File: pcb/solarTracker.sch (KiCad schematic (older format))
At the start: 11 parts, among them U1 photodiode, U2 photodiode, U3 MCP6494, U4 photodiode, U5 photodiode

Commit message: use stm32d100 mcu, switch between four analog inputs using multiplexer, separate analog and digital gnds
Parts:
- added C3, C4, C5, C6, C7: C, symbol C
- added U6: STM32F071CBT6, symbol STM32F071CBT6
- U1, U2, U4, U5: symbol photodiode -> photodiode-RESCUE-solarTracker
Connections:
- net labels added: +BATT, DIO1, DIO2, DIO3, DIO4
- wire segments 47 -> 50
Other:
- moved on the sheet: C1, C2, R1, R2, R3, R4

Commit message: add 2nd order Butterworth filter, change first amp to lm324
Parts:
- removed R1, R2, R3, R4: UNREGULATED, symbol R
- removed U1, U2, U4, U5: photodiode, symbol photodiode-RESCUE-solarTracker
- removed U3: MCP6494, symbol MCP6494
- added C3, C4, C5: C, symbol C
- added U1: 74HC4052, symbol 74HC4052
- C2: value 100n -> C
- renumbered C7 to C10, C3 to C6, C4 to C7, C5 to C8, C6 to C9, U6 to U2
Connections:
- net labels added: GNDA
- net labels removed: +BATT, DIO1, DIO2, DIO3, DIO4, GND
- wire segments 50 -> 54
- no-connect marks 0 -> 5
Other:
- moved on the sheet: C10, C6, C7, C8, C9, U2

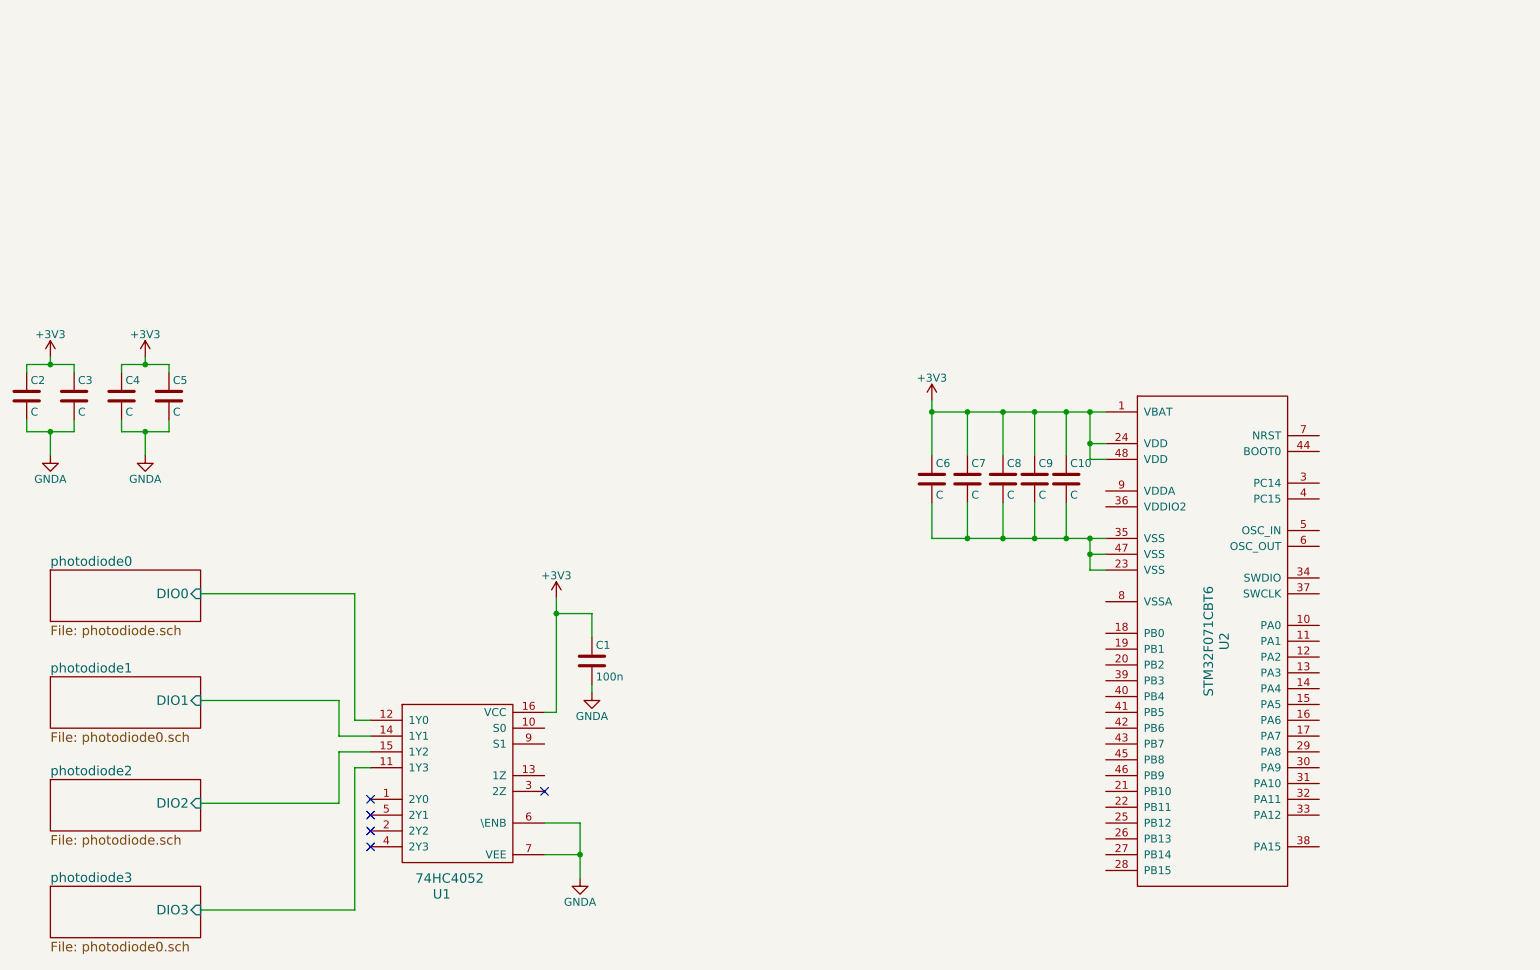
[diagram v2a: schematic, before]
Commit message: fix hierachal sheet labelling
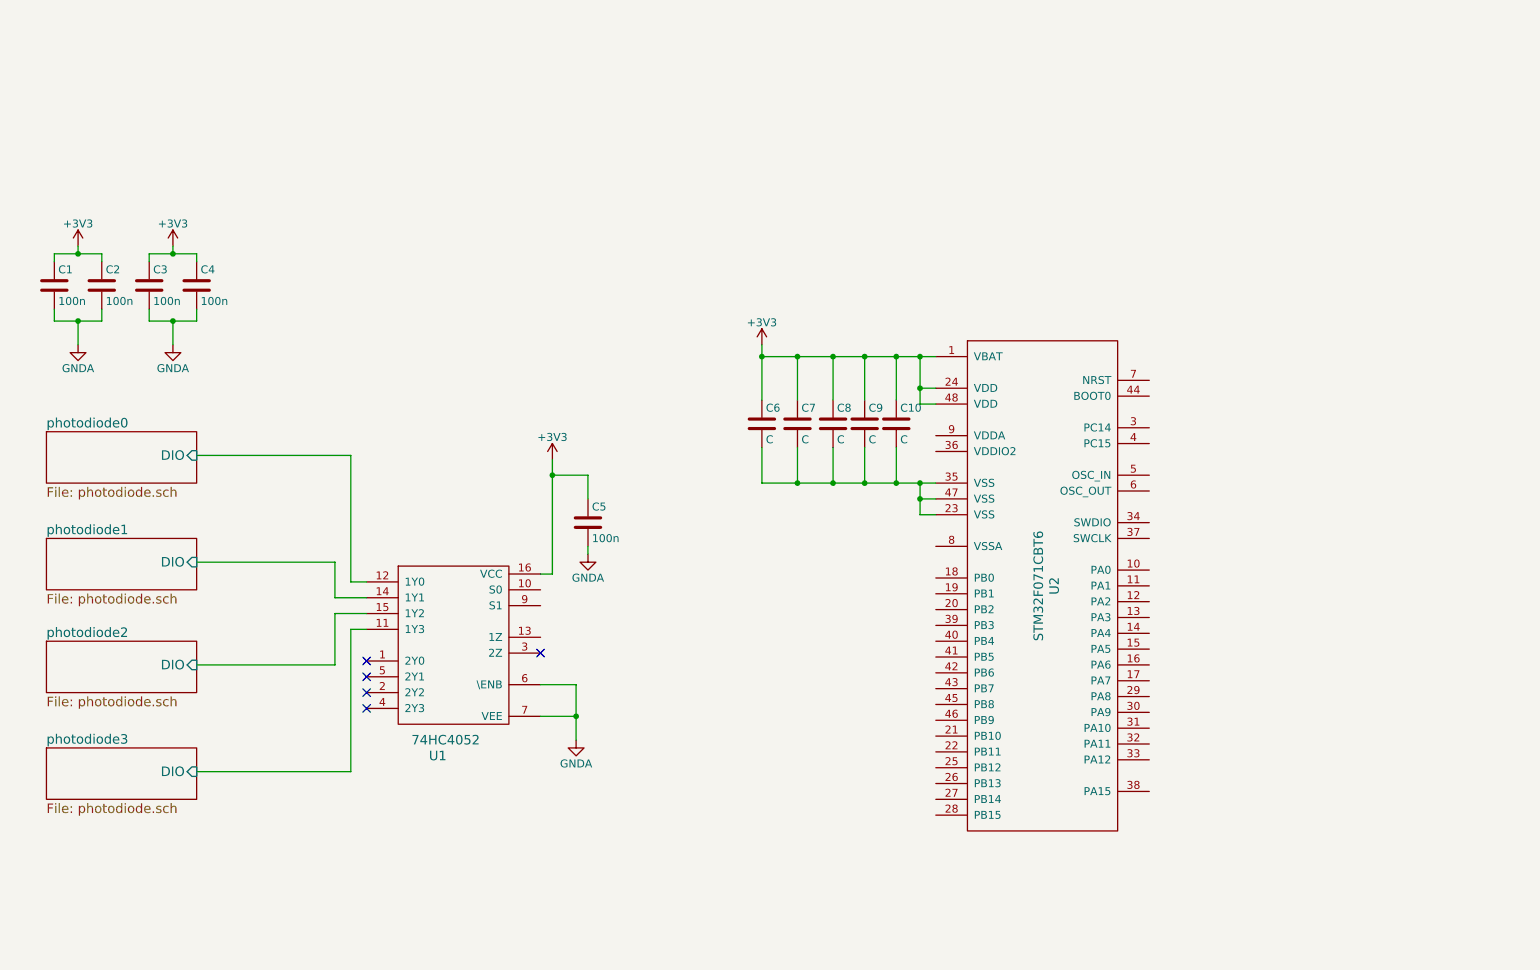
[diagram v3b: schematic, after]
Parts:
- C1: renamed from C2; value C -> 100n
- C2: renamed from C3; value C -> 100n
- C3: renamed from C4; value C -> 100n
- C4: renamed from C5; value C -> 100n
- renumbered C1 to C5
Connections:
- net photodiode0/DIO0 renamed photodiode0/DIO
- net photodiode1/DIO1 renamed photodiode1/DIO
- net photodiode2/DIO2 renamed photodiode2/DIO
- net photodiode3/DIO3 renamed photodiode3/DIO
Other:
- moved on the sheet: C1, C10, C2, C3, C4, C5, C6, C7, C8, C9, U1, U2

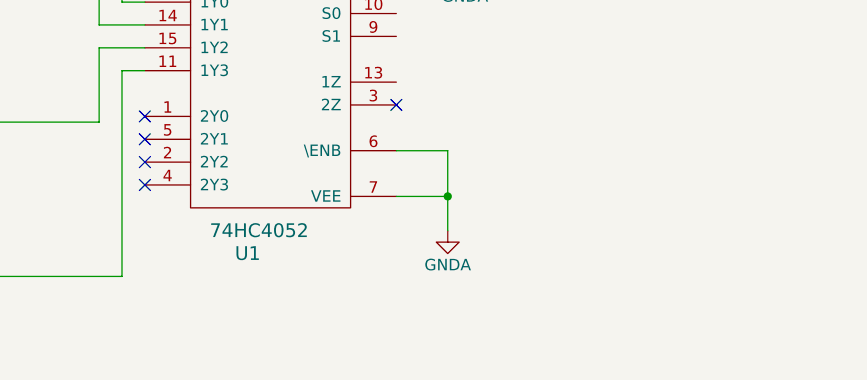
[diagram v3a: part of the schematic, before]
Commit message: change filter resistor to correct value, reduce cap size (and cost)
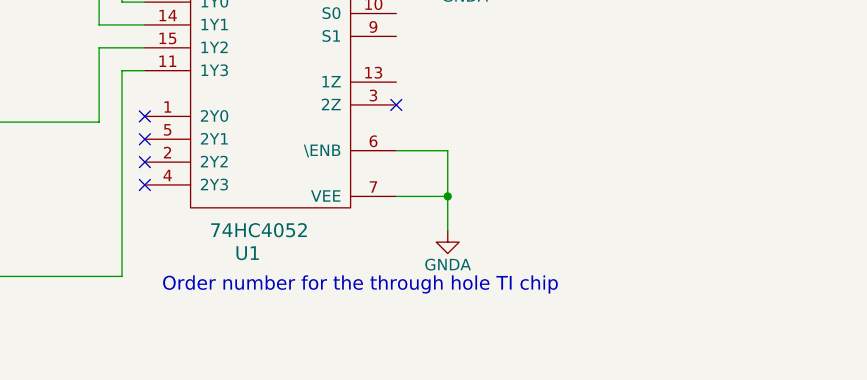
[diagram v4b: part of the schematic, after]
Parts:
- C3: Order No (none) -> 2468845; Supplier (none) -> Farnell
- U1: Order No (none) -> 1740159; Supplier (none) -> Farnell
- U2: Order No (none) -> 2376483; Supplier (none) -> Farnell
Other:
- note added: "Order number for the through hole TI chip"
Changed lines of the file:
@@
 F 2 "" H 7600 4725 60  0000 C CNN
 F 3 "" H 7600 4725 60  0000 C CNN
+F 4 "Farnell" V 7600 4525 60  0001 C CNN "Supplier"
+F 5 "2376483" V 7600 4525 60  0001 C CNN "Order No"
 	1    7600 4525
 	1    0    0    -1
@@
 F 2 "" H 3750 5450 60  0000 C CNN
 F 3 "" H 3750 5450 60  0000 C CNN
+F 4 "Farnell" H 3750 5450 60  0001 C CNN "Supplier"
+F 5 "1740159" H 3750 5450 60  0001 C CNN "Order No"
 	1    3750 5450
 	1    0    0    -1
 $EndComp
 $Comp
-L +3V3 #PWR5
+L +3V3 #PWR01
 U 1 1 55BCF6B7
 P 4475 3575
-F 0 "#PWR5" H 4475 3425 50  0001 C CNN
+F 0 "#PWR01" H 4475 3425 50  0001 C CNN
 F 1 "+3V3" H 4475 3715 50  0000 C CNN
 F 2 "" H 4475 3575 60  0000 C CNN
@@
 NoConn ~ 4400 4800
 $Comp
-L +3V3 #PWR8
+L +3V3 #PWR02
 U 1 1 55BD10C3
 P 5800 2850
-F 0 "#PWR8" H 5800 2700 50  0001 C CNN
+F 0 "#PWR02" H 5800 2700 50  0001 C CNN
 F 1 "+3V3" H 5800 2990 50  0000 C CNN
 F 2 "" H 5800 2850 60  0000 C CNN
@@
 $EndComp
 $Comp
-L GNDA #PWR6
+L GNDA #PWR03
 U 1 1 55BD2327
 P 4625 5350
-F 0 "#PWR6" H 4625 5100 50  0001 C CNN
+F 0 "#PWR03" H 4625 5100 50  0001 C CNN
 F 1 "GNDA" H 4625 5200 50  0000 C CNN
 F 2 "" H 4625 5350 60  0000 C CNN
@@
 $EndComp
 $Comp
-L GNDA #PWR7
+L GNDA #PWR04
 U 1 1 55BD23CA
 P 4700 4175
-F 0 "#PWR7" H 4700 3925 50  0001 C CNN
+F 0 "#PWR04" H 4700 3925 50  0001 C CNN
 F 1 "GNDA" H 4700 4025 50  0000 C CNN
 F 2 "" H 4700 4175 60  0000 C CNN
@@
 $EndComp
 $Comp
-L +3V3 #PWR1
+L +3V3 #PWR05
 U 1 1 55BD678A
 P 1475 2225
-F 0 "#PWR1" H 1475 2075 50  0001 C CNN
+F 0 "#PWR05" H 1475 2075 50  0001 C CNN
 F 1 "+3V3" H 1475 2365 50  0000 C CNN
 F 2 "" H 1475 2225 60  0000 C CNN
@@
 $EndComp
 $Comp
-L GNDA #PWR2
+L GNDA #PWR06
 U 1 1 55BD793E
 P 1475 2850
-F 0 "#PWR2" H 1475 2600 50  0001 C CNN
+F 0 "#PWR06" H 1475 2600 50  0001 C CNN
 F 1 "GNDA" H 1475 2700 50  0000 C CNN
 F 2 "" H 1475 2850 60  0000 C CNN
@@
 $EndSheet
 $Comp
-L +3V3 #PWR3
+L +3V3 #PWR07
 U 1 1 55BDA963
 P 2075 2225
-F 0 "#PWR3" H 2075 2075 50  0001 C CNN
+F 0 "#PWR07" H 2075 2075 50  0001 C CNN
 F 1 "+3V3" H 2075 2365 50  0000 C CNN
 F 2 "" H 2075 2225 60  0000 C CNN
@@
 F 2 "" H 1963 2325 30  0000 C CNN
 F 3 "" H 1925 2475 60  0000 C CNN
+F 4 "Farnell" H 1925 2475 60  0001 C CNN "Supplier"
+F 5 "2468845" H 1925 2475 60  0001 C CNN "Order No"
 	1    1925 2475
 	1    0    0    -1
 $EndComp
 $Comp
-L GNDA #PWR4
+L GNDA #PWR08
 U 1 1 55BDA97F
 P 2075 2850
-F 0 "#PWR4" H 2075 2600 50  0001 C CNN
+F 0 "#PWR08" H 2075 2600 50  0001 C CNN
 F 1 "GNDA" H 2075 2700 50  0000 C CNN
 F 2 "" H 2075 2850 60  0000 C CNN
@@
 Wire Wire Line
 	3200 5550 2225 5550
+Text Notes 3375 5625 0    60   ~ 0
+Order number for the through hole TI chip
 $EndSCHEMATC

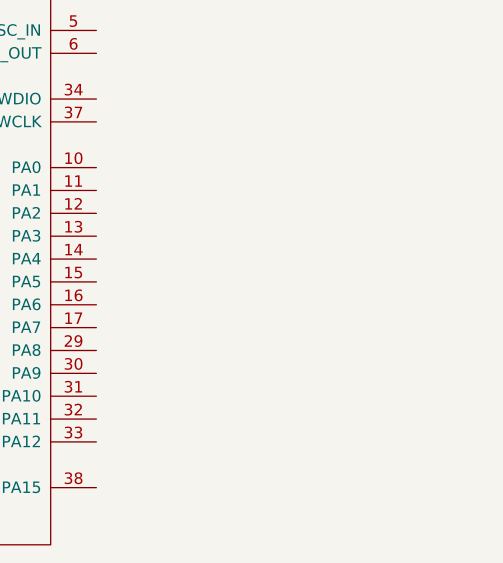
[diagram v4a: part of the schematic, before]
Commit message: add servo
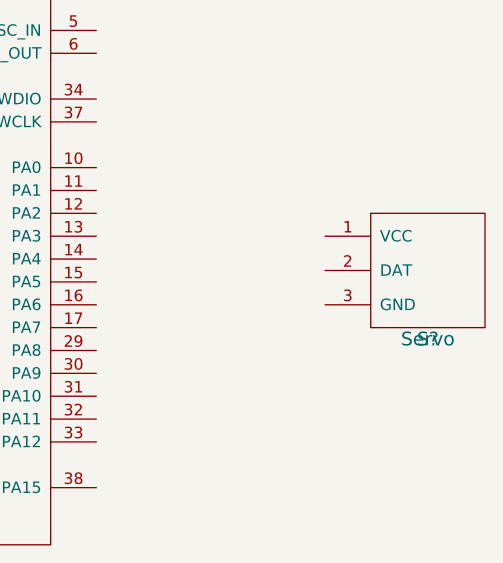
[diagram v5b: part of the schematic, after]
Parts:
- added S?: Servo, symbol Servo
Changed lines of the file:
@@
 LIBS:stm32f071cbt6
 LIBS:74hc4052
+LIBS:servo
 LIBS:solarTracker-cache
 EELAYER 25 0
@@
 Text Notes 3375 5625 0    60   ~ 0
 Order number for the through hole TI chip
+$Comp
+L Servo S?
+U 1 1 55BE7FEA
+P 9700 5025
+F 0 "S?" H 9700 5025 60  0000 C CNN
+F 1 "Servo" H 9700 5025 60  0000 C CNN
+F 2 "" H 9700 5025 60  0000 C CNN
+F 3 "" H 9700 5025 60  0000 C CNN
+	1    9700 5025
+	1    0    0    -1
+$EndComp
 $EndSCHEMATC

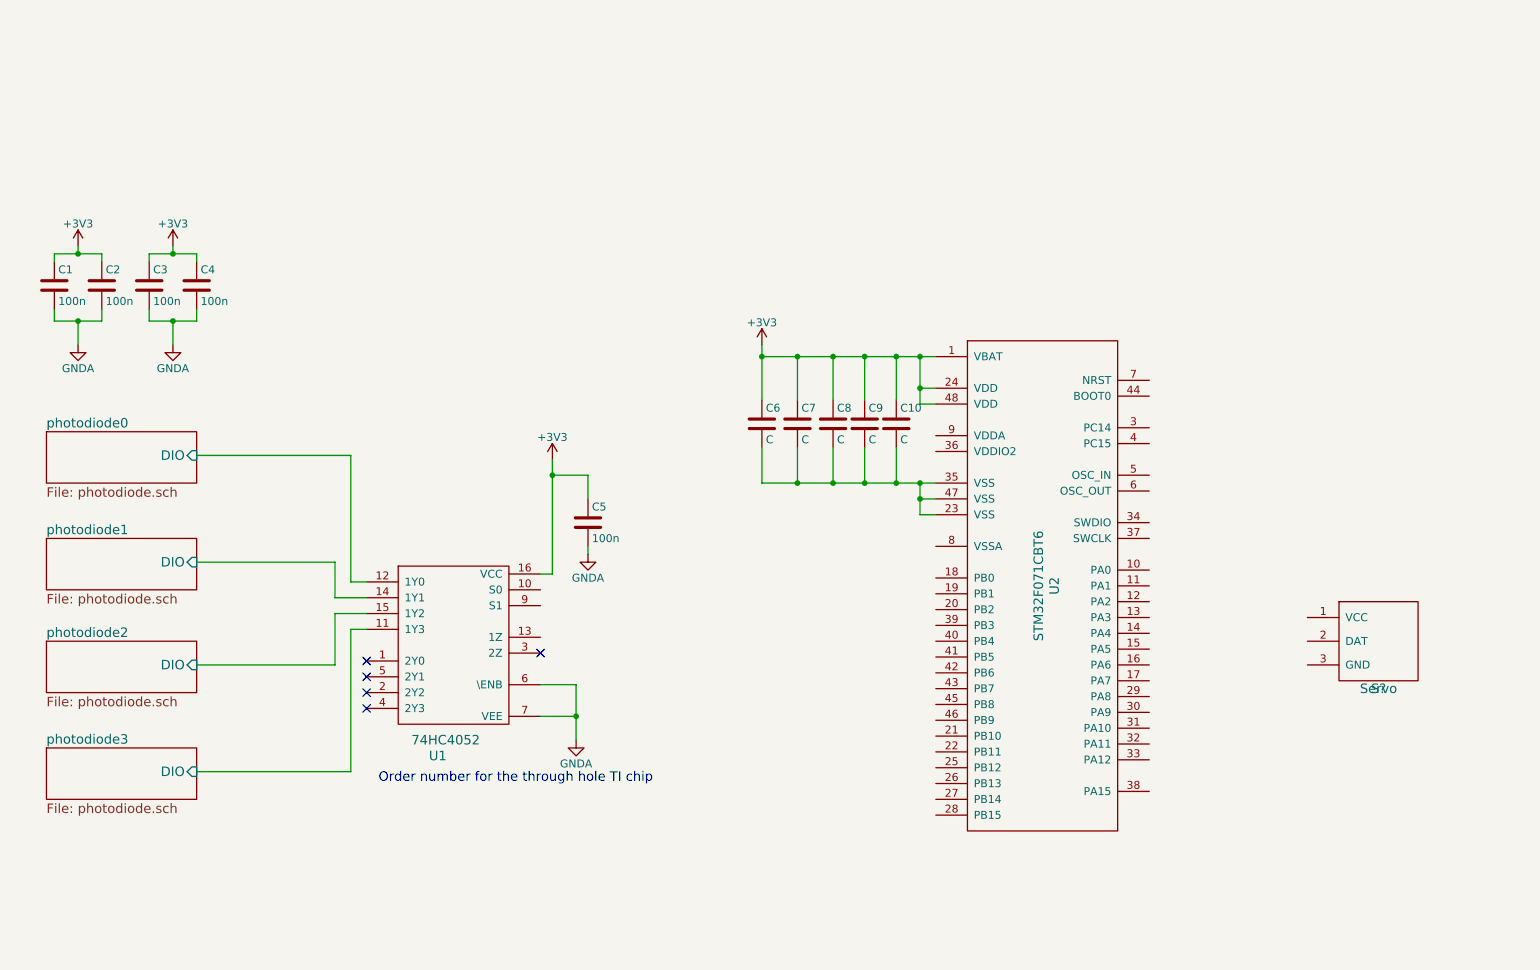
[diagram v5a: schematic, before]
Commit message: 6V converter for servo power
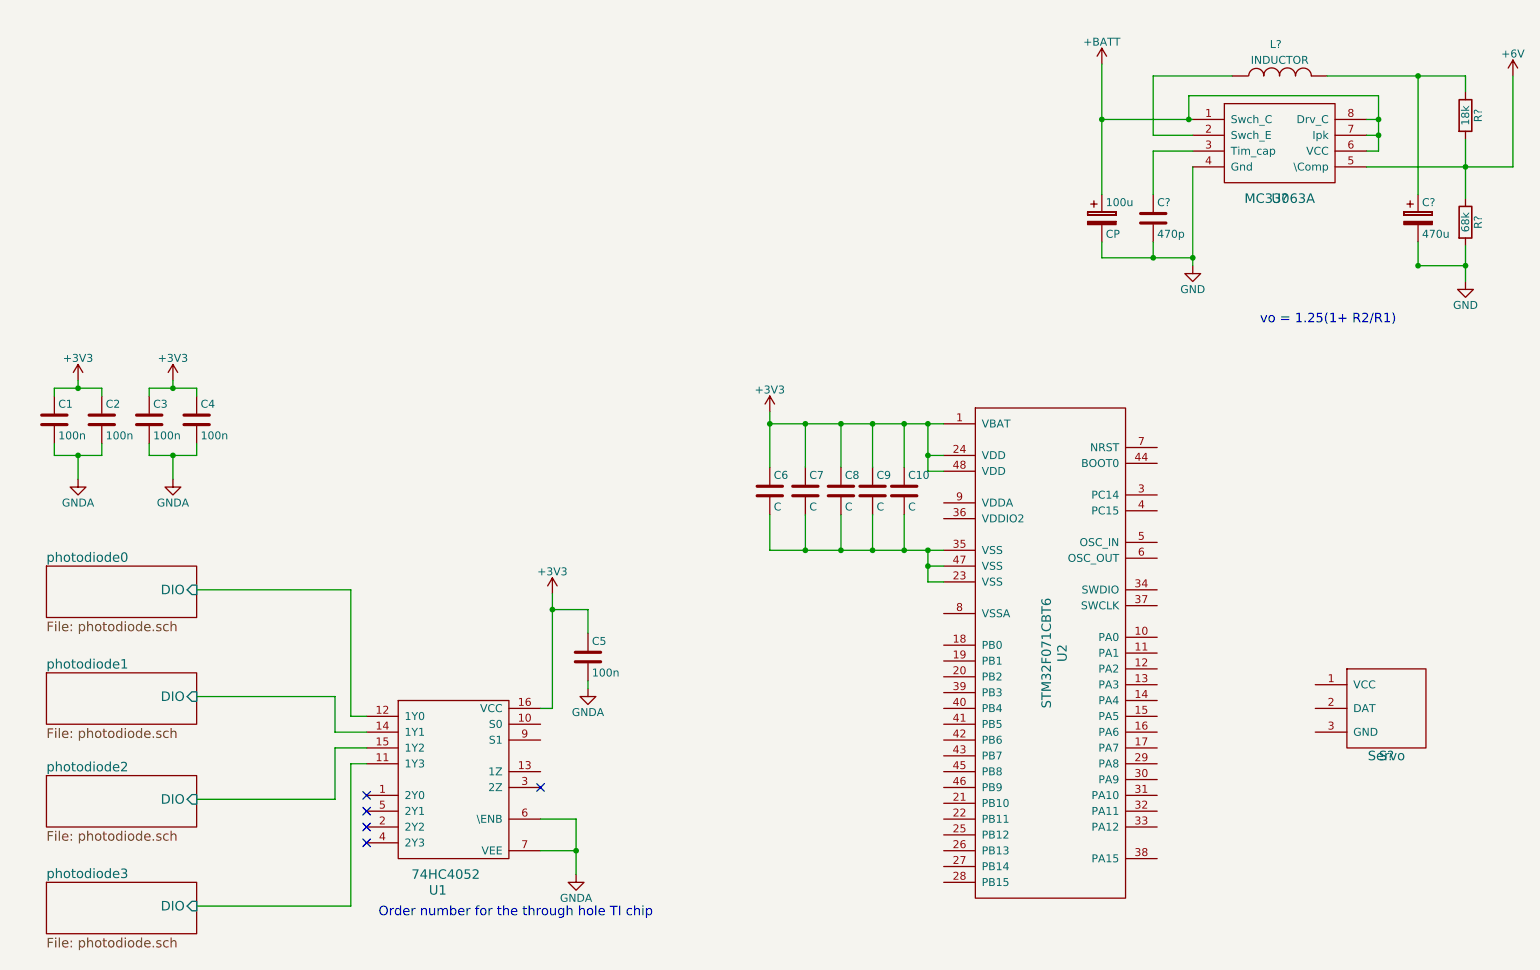
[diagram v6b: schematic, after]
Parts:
- added 100u: CP, symbol CP
- added C?: 470u, symbol CP
- added C?: 470p, symbol C
- added L?: INDUCTOR, symbol INDUCTOR
- added R?: 18k, symbol R
- added R?: 68k, symbol R
- added U?: MC33063A, symbol MC33063A
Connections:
- new net: L?.1, U?.2 (Swch_E)
- new net: C?.1, U?.3 (Tim_cap)
- new net: C?.1, L?.2, R?.1
- new net +6V: R?.1, R?.2, U?.5 (\Comp)
- new net +BATT: 100u.1, U?.1 (Swch_C), U?.6 (VCC), U?.7 (Ipk), U?.8 (Drv_C)
- new net GND: 100u.2, C?.2, C?.2, R?.2, U?.4 (Gnd)
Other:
- note added: "vo = 1.25(1+ R2/R1)"
- moved on the sheet: C1, C10, C2, C3, C4, C5, C6, C7, C8, C9, S?, U1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

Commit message: finish power circuit
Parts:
- added D?: 1N5819, symbol D_Schottky
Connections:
- net +6V: now also S?.1 (VCC)
- net +BATT: now also L?.1
- net GND: now also S?.3 (GND), U?.2 (Swch_E)
- net at C?.1, R?.1: now also D?.1 (K); no longer L?.2
- new net: D?.2 (A), L?.2
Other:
- moved on the sheet: 100u, C?, L?
